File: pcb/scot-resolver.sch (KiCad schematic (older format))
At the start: 15 parts, among them J1 Conn_01x02_Female, J2 Conn_01x03_Female, J3 Conn_01x03_Female, J4 Conn_01x03_Female, J5 Conn_01x02_Female, J6 Conn_01x02_Female, J8 Conn_01x02_Female

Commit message: pcb: Progress on v2 layout.
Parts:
- removed TP4, TP5: TestPoint, TestPoint:TestPoint_Pad_D1.5mm, symbol Connector:TestPoint
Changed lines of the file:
@@
 Wire Wire Line
 	1550 1150 2200 1150
-Wire Wire Line
-	9950 1550 9400 1550
-Wire Wire Line
-	9300 1650 9400 1650
 $Sheet
 S 7550 4200 1750 450
@@
 F12 "5V_RESOLVER_ANALOGUE" I L 4400 2400 50
 F13 "5V_RESOLVER_DIGITAL" I L 4400 2550 50
+F14 "0V_ANALOGUE" I L 4400 3600 50
+F15 "0V_DIGITAL" I L 4400 3750 50
 $EndSheet
 Wire Wire Line
@@
 Wire Wire Line
 	4000 3150 3550 3150
-Wire Wire Line
-	3550 3300 4150 3300
 Wire Wire Line
 	4150 3300 4150 3100
@@
 	7250 2950 7550 2950
 $Comp
-L Connector:TestPoint TP4
-U 1 1 5EA9AA55
-P 9400 1550
-F 0 "TP4" H 9458 1668 50  0000 L CNN
-F 1 "TestPoint" H 9458 1577 50  0000 L CNN
-F 2 "TestPoint:TestPoint_Pad_D1.5mm" H 9600 1550 50  0001 C CNN
-F 3 "~" H 9600 1550 50  0001 C CNN
-	1    9400 1550
-	1    0    0    -1
-$EndComp
-Connection ~ 9400 1550
-Wire Wire Line
-	9400 1550 9300 1550
-$Comp
-L Connector:TestPoint TP5
-U 1 1 5EA9B1EC
-P 9400 1650
-F 0 "TP5" H 9342 1676 50  0000 R CNN
-F 1 "TestPoint" H 9342 1767 50  0000 R CNN
-F 2 "TestPoint:TestPoint_Pad_D1.5mm" H 9600 1650 50  0001 C CNN
-F 3 "~" H 9600 1650 50  0001 C CNN
-	1    9400 1650
-	-1   0    0    1
-$EndComp
-Connection ~ 9400 1650
-Wire Wire Line
-	9400 1650 9950 1650
-$Comp
 L power:GNDA #PWR0115
 U 1 1 5EAA1A37
@@
 	1    0    0    -1
 $EndComp
+Wire Wire Line
+	3550 3300 4150 3300
+Wire Wire Line
+	4400 3600 3950 3600
+Wire Wire Line
+	3950 3600 3950 1400
+Wire Wire Line
+	3950 1400 3550 1400
+Wire Wire Line
+	3550 1950 3900 1950
+Wire Wire Line
+	3900 1950 3900 3750
+Wire Wire Line
+	3900 3750 4400 3750
+Wire Wire Line
+	9300 1550 9950 1550
+Wire Wire Line
+	9300 1650 9950 1650
 $EndSCHEMATC

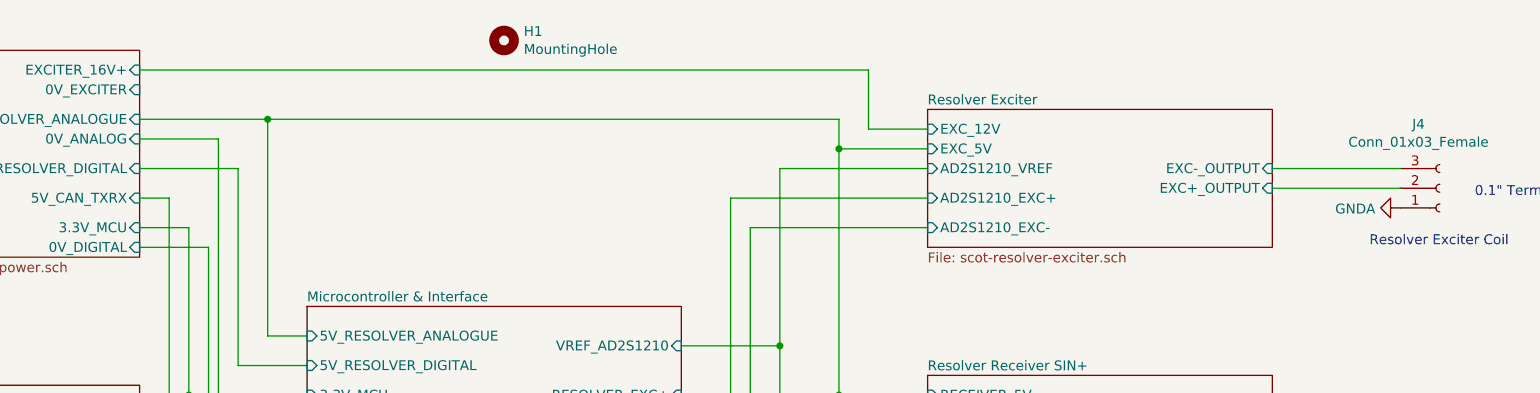
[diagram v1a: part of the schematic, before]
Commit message: pcb: Clear up exciter ground rail (sch & pcb).
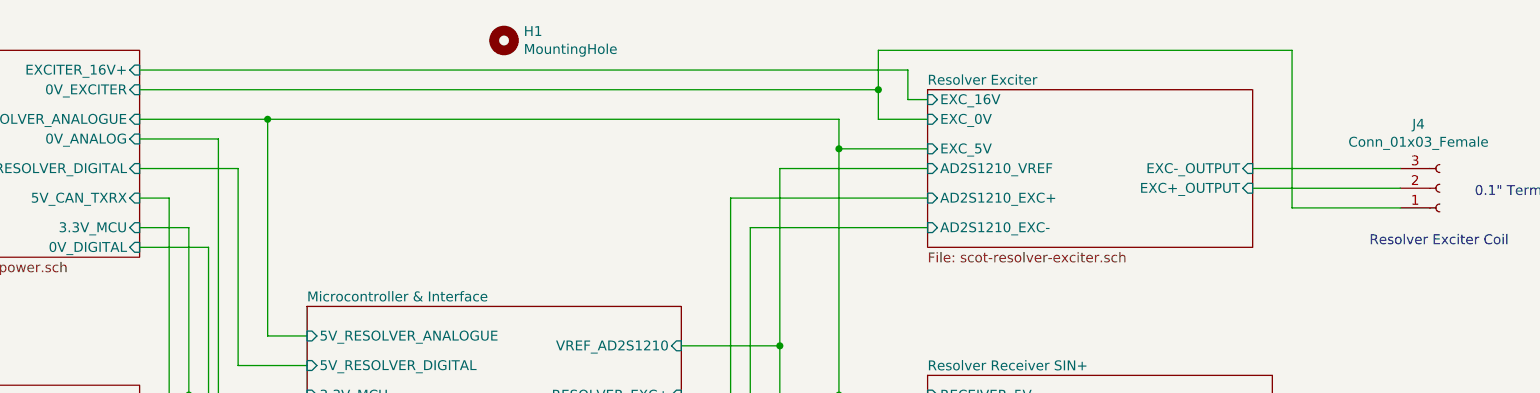
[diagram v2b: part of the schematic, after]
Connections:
- net GNDA: no longer J4.1 (Pin_1)
- net Power Supplies/0V_EXCITER: now also J4.1 (Pin_1)
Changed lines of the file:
@@
 	1700 2600 1550 2600
-$Sheet
-S 7550 1250 1750 700
-U 5E0AB524
-F0 "Resolver Exciter" 50
-F1 "scot-resolver-exciter.sch" 50
-F2 "AD2S1210_VREF" I L 7550 1550 50
-F3 "EXC+_OUTPUT" I R 9300 1650 50
-F4 "EXC-_OUTPUT" I R 9300 1550 50
-F5 "AD2S1210_EXC+" I L 7550 1700 50
-F6 "AD2S1210_EXC-" I L 7550 1850 50
-F7 "EXC_12V" I L 7550 1350 50
-F8 "EXC_5V" I L 7550 1450 50
-$EndSheet
 $Sheet
 S 7550 2600 1750 450
@@
 Wire Wire Line
 	3700 2750 3550 2750
-Wire Wire Line
-	3550 1050 7250 1050
-Wire Wire Line
-	7250 1050 7250 1350
-Wire Wire Line
-	7250 1350 7550 1350
 Wire Wire Line
 	7100 1300 7100 1450
@@
 	4050 1550 3550 1550
 $Comp
-L power:GNDA #PWR0101
-U 1 1 5E620224
-P 9950 1750
-F 0 "#PWR0101" H 9950 1500 50  0001 C CNN
-F 1 "GNDA" V 9955 1623 50  0000 R CNN
-F 2 "" H 9950 1750 50  0001 C CNN
-F 3 "" H 9950 1750 50  0001 C CNN
-	1    9950 1750
-	0    1    1    0
-$EndComp
-$Comp
 L power:GNDA #PWR0102
 U 1 1 5E62D3A8
@@
 Wire Wire Line
 	3900 3750 4400 3750
-Wire Wire Line
-	9300 1550 9950 1550
-Wire Wire Line
-	9300 1650 9950 1650
+$Sheet
+S 7550 1150 1650 800
+U 5E0AB524
+F0 "Resolver Exciter" 50
+F1 "scot-resolver-exciter.sch" 50
+F2 "AD2S1210_VREF" I L 7550 1550 50
+F3 "EXC+_OUTPUT" I R 9200 1650 50
+F4 "EXC-_OUTPUT" I R 9200 1550 50
+F5 "AD2S1210_EXC+" I L 7550 1700 50
+F6 "AD2S1210_EXC-" I L 7550 1850 50
+F7 "EXC_5V" I L 7550 1450 50
+F8 "EXC_16V" I L 7550 1200 50
+F9 "EXC_0V" I L 7550 1300 50
+$EndSheet
+Wire Wire Line
+	9200 1550 9950 1550
+Wire Wire Line
+	9200 1650 9950 1650
+Wire Wire Line
+	7450 1050 7450 1200
+Wire Wire Line
+	7450 1200 7550 1200
+Wire Wire Line
+	3550 1050 7450 1050
+Wire Wire Line
+	7550 1300 7300 1300
+Wire Wire Line
+	7300 1300 7300 1150
+Wire Wire Line
+	7300 1150 3550 1150
+Wire Wire Line
+	7300 1150 7300 950
+Wire Wire Line
+	7300 950  9400 950
+Wire Wire Line
+	9400 950  9400 1750
+Wire Wire Line
+	9400 1750 9950 1750
+Connection ~ 7300 1150
 $EndSCHEMATC
